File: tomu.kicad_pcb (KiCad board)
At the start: 2 copper layers, 13 x 11 mm, 16 parts, among them P1 USART0, P2 DEBUG, P3 USB-PCB, U1 EFM32HG309

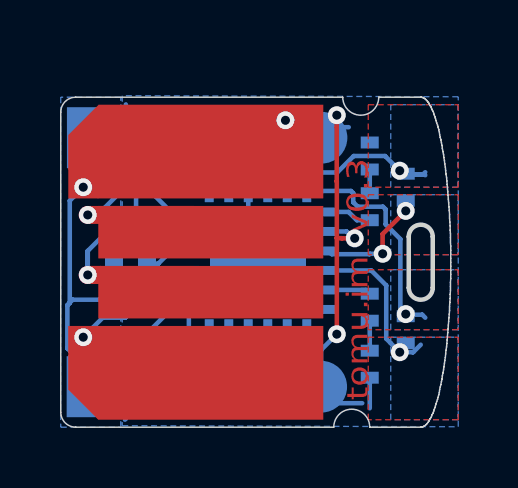
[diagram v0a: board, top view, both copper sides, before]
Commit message: wip commit: half-done rework
The big difference with v0.4 is a large cutout on the side to facilitate
mating with an enclosure.  This necessitates many changes to the board
layout.

Signed-off-by: Sean Cross <sean@xobs.io>
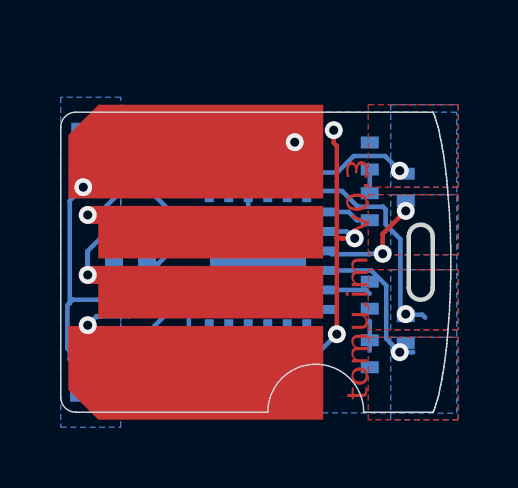
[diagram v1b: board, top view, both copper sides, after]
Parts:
- P1: footprint debug-points -> usb-pcb:SMT-4pin
- moved R2 0.40 mm to (27.3, 24.6)
- moved D2 0.35 mm to (27.3, 26.6)
- moved P2 0.25 mm to (18.1, 19.6)
- moved P1 0.25 mm to (18.1, 27.4)
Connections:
- P1 pad 4: +3V3 -> (no net)
- P2 pad 4: +3V3 -> Net-(P2-Pad4)
- U1 pad 7: Net-(U1-Pad7) -> Net-(P2-Pad4)
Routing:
- net +3V3: track 33.7 -> 22.5 mm
- net GND: track 31.4 -> 29.0 mm
- net /USB_5V: track 10.9 -> 9.51 mm
- net /CAP0B: track 6.25 -> 5.21 mm
- net Net-(D2-Pad1): track 1.00 -> 0.00 mm
- net (no net): track 0.00 -> 1.00 mm
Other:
- board size 13 x 11 mm -> 13 x 10 mm
